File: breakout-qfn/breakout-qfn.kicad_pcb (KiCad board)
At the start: 2 copper layers, 50 x 52 mm, 153 parts, among them J1 Conn_01x04, J10 U.FL, J11 U.FL, J12 U.FL, J13 U.FL, J2 U.FL, J3 U.FL, J4 U.FL, J5 U.FL, J6 U.FL, J7 U.FL, J8 U.FL, J9 U.FL, U1 Openframe_QFN_TT06_REV2, U2 24LC02

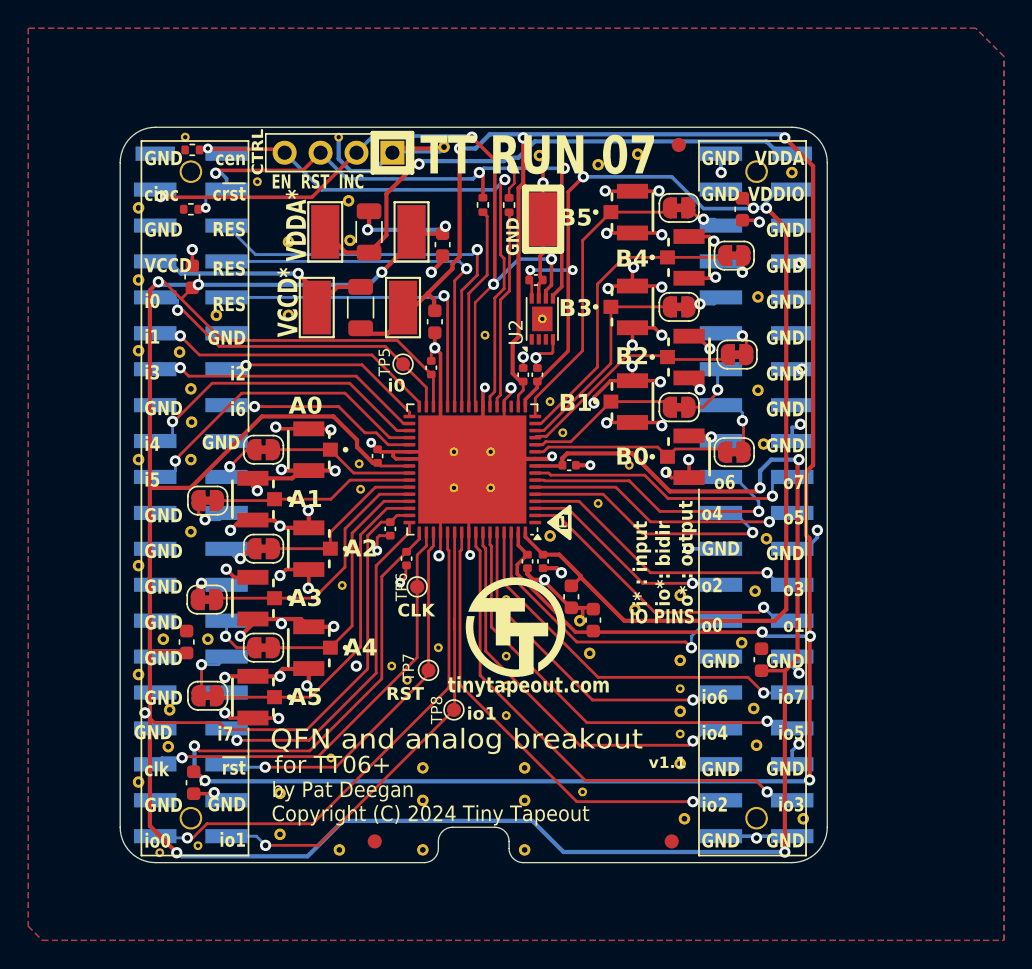
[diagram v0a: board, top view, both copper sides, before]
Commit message: TT08 breakout and documentation refactor
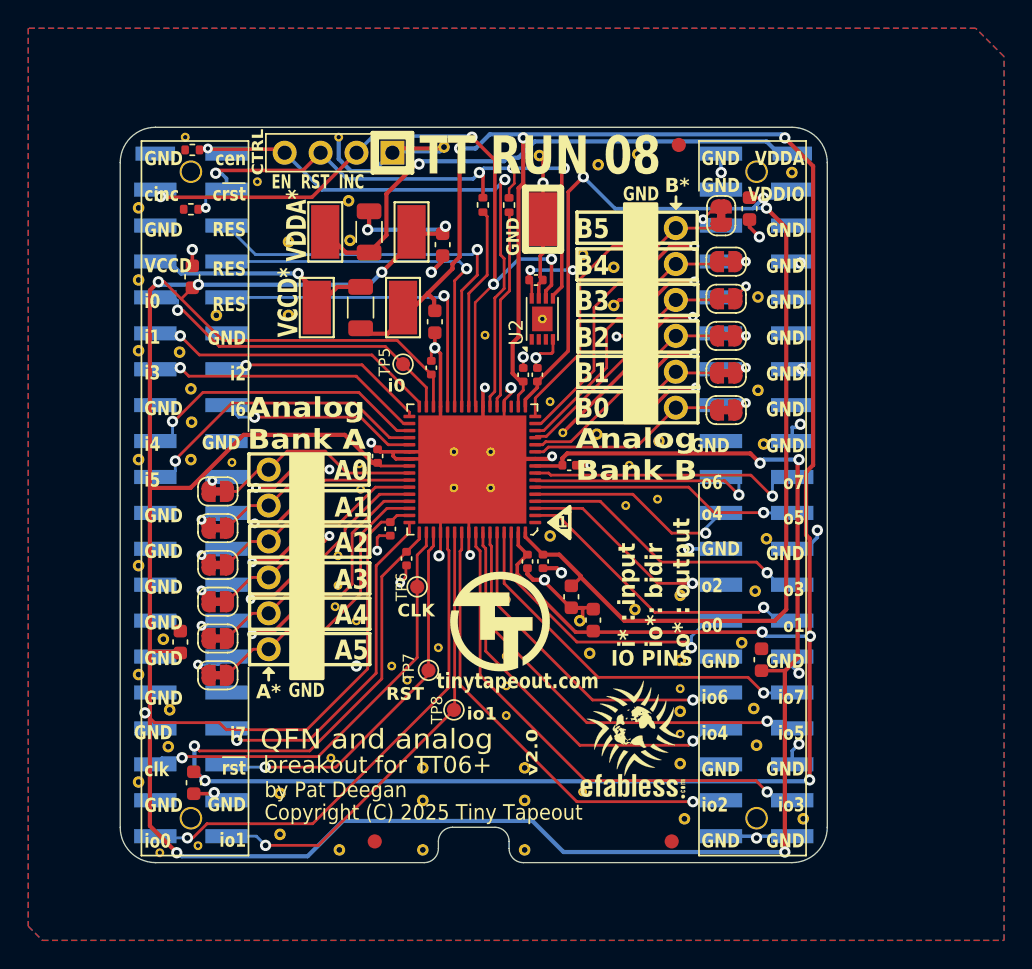
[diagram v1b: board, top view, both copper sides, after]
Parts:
- removed J10, J11, J12, J13, J4, J5, J6, J7, J8, J9: U.FL, psysnapeda:SAMTEC_RSP-122811-01
- removed the STITCHB1 at (50.5, 46.6)
- removed the STITCHB1 at (51.7, 54.2)
- added EFABLOG: Logo, TinyTapeout:ef_logo_graphical, F.Cu at (81.8, 60.5)
- added EFABLOG: Logo, TinyTapeout:ef_logo_graphical, B.Cu at (71.7, 64.1)
- added EFABTXT: Logo, TinyTapeout:ef_logo, F.Cu at (81.7, 64.6)
- added EFABTXT: Logo, TinyTapeout:ef_logo, B.Cu at (71.7, 60.0)
- added STITCHB1: StitchingVia-0.4mmDrill, flyingcarsfootprints:StitchingVia-0.4mmDrill, F.Cu at (83.6, 40.2)
- added STITCHB1: StitchingVia-0.4mmDrill, flyingcarsfootprints:StitchingVia-0.4mmDrill, F.Cu at (79.2, 39.7)
- added STITCHB1: StitchingVia-0.4mmDrill, flyingcarsfootprints:StitchingVia-0.4mmDrill, F.Cu at (80.4, 30.6)
- added STITCHB1: StitchingVia-0.4mmDrill, flyingcarsfootprints:StitchingVia-0.4mmDrill, F.Cu at (78.2, 27.0)
- added STITCHB1: StitchingVia-0.4mmDrill, flyingcarsfootprints:StitchingVia-0.4mmDrill, F.Cu at (80.4, 27.9)
- added STITCHM1: StitchingVia-0.3mm, flyingcarsfootprints:StitchingVia-0.3mm, F.Cu at (83.5, 44.3)
- added STITCHM1: StitchingVia-0.3mm, flyingcarsfootprints:StitchingVia-0.3mm, F.Cu at (60.9, 48.3)
- added STITCHM1: StitchingVia-0.3mm, flyingcarsfootprints:StitchingVia-0.3mm, F.Cu at (62.2, 52.9)
- added STITCHM1: StitchingVia-0.3mm, flyingcarsfootprints:StitchingVia-0.3mm, F.Cu at (53.4, 41.7)
- added STITCHM1: StitchingVia-0.3mm, flyingcarsfootprints:StitchingVia-0.3mm, F.Cu at (60.7, 51.9)
- J2, J3: value U.FL -> Conn_02x06_Odd_Even; footprint psysnapeda:SAMTEC_RSP-122811-01 -> Connector_PinHeader_2.54mm:PinHeader_2x06_P2.54mm_Vertical
- JP1, JP10, JP11, JP12, JP2, JP3, JP4, JP5, JP6, JP7, JP8, JP9: footprint Jumper:SolderJumper-2_P1.3mm_Bridged_RoundedPad1.0x1.5mm -> TinyTapeout:SolderJumper-2_P1.3mm_Bridged_RoundedPad1.0x1.5mmEasyCut
- moved J3 33.4 mm to (82.2, 25.1), turned to 0 degrees
- moved J2 14.1 mm to (58.5, 54.9), turned to 180 degrees
- moved JP1 4.38 mm to (52.4, 43.8)
- moved JP8 4.12 mm to (88.3, 35.4)
- moved JP3 3.44 mm to (52.4, 49.0)
- moved JP10 3.37 mm to (88.3, 30.1)
- moved JP5 3.30 mm to (52.4, 54.1)
- moved JP7 3.03 mm to (88.3, 38.0)
- moved JP12 3.03 mm to (88.0, 24.2), turned to 90 degrees
- moved Z2ALOGO01 2.81 mm to (61.4, 62.2)
- moved TTLOGO01 2.11 mm to (80.9, 62.6)
- moved JP2 2.08 mm to (52.4, 46.4)
- moved STITCHM1 1.96 mm to (81.2, 44.8)
- moved JP6 1.62 mm to (52.4, 56.8)
- moved JP9 1.54 mm to (88.3, 32.8)
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- renumbered REF** to TTLOGO01, REF** to Z2ALOGO01
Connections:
- J2 pad 1: /chip_an0 -> GND
- J3 pad 1: /chip_an1 -> GND
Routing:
- net GND: track 206.7 -> 180.3 mm, vias 69 -> 42
- net /uout4: track 19.5 -> 15.1 mm
- net /chip_an0: track 10.3 -> 14.7 mm
- net vdda_all: track 250.1 -> 245.9 mm
- net /chip_an7: track 11.0 -> 15.0 mm
- net /uout6: track 20.8 -> 17.2 mm
- net /chip_an5: track 23.8 -> 20.2 mm
- net /chip_an2: track 12.1 -> 15.2 mm
- net /chip_an9: track 15.5 -> 18.3 mm
- net /chip_an3: track 18.3 -> 16.3 mm
- net /chip_an11: track 21.0 -> 22.6 mm
- net /chip_an10: track 21.8 -> 20.2 mm
- net /chip_an4: track 17.8 -> 19.0 mm
- net /hd_an7: track 4.25 -> 3.05 mm
- net /hd_an0: track 3.06 -> 1.98 mm
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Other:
- board text added: "A*"
- board text added: "Analog Bank A"
- board text added: "Analog Bank B"
- board text added: "B*"
- board text added: "Copyright (C) 2025 Tiny Tapeout"
- board text added: "MUX CTRL"
- board text added: "QFN and analog"
- board text added: "TT RUN 08"
- board text added: "TT06+ QFN breakout v2"
- board text added: "TinyTapeout designs are packaged together along with a MUX that allows for directing I/O to any"
- board text added: "breakout for TT06+"
- board text added: "selected project, controlled through the cinc, cen and c~{rst} pins. This PCB provides a way to deliver these chips that will sit atop the demo board, but also allows you to easily integrate the ICs into your own projects. For details, see"
- board text added: "v2.0"
- board text removed: "Copyright (C) 2024 Tiny Tapeout"
- board text removed: "QFN and analog breakout"
- board text removed: "TT RUN 07"
- board text removed: "TT06+ QFN breakout v1"
- board text removed: "TinyTapeout designs are packaged together along with a MUX that allows for directing I/O to any selected project, controlled through the cinc, cen and c~{rst} pins. This PCB provides a way to deliver these chips that will sit atop the demo board, but also allows you to easily integrate the ICs into your own projects. For details, see"
- board text removed: "for TT06+"
- board text removed: "v1.1"

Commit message: minor routing tweaks and stitch
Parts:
- added STITCHB1: StitchingVia-0.4mmDrill, flyingcarsfootprints:StitchingVia-0.4mmDrill, F.Cu at (70.3, 60.8)
- added STITCHB1: StitchingVia-0.4mmDrill, flyingcarsfootprints:StitchingVia-0.4mmDrill, F.Cu at (58.2, 59.6)
- added STITCHB1: StitchingVia-0.4mmDrill, flyingcarsfootprints:StitchingVia-0.4mmDrill, F.Cu at (50.3, 44.4)
- added STITCHM1: StitchingVia-0.3mm, flyingcarsfootprints:StitchingVia-0.3mm, F.Cu at (77.8, 45.7)
- added STITCHM1: StitchingVia-0.3mm, flyingcarsfootprints:StitchingVia-0.3mm, F.Cu at (79.3, 45.2)
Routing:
- net GND: track 180.3 -> 194.5 mm
- net vdda_in: track 39.0 -> 40.1 mm
- net vccd_in: track 17.1 -> 18.0 mm
- net /uio1: track 33.8 -> 33.0 mm
- net vdda_all: track 245.9 -> 245.2 mm, vias 10 -> 9

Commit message: routing tweaks
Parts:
- moved STITCHB1 1.45 mm to (88.0, 54.5)
- moved STITCHB1 0.65 mm to (90.5, 47.1)
- moved STITCHB1 0.47 mm to (90.5, 40.2)
- moved STITCHB1 0.38 mm to (93.5, 66.8)
- moved STITCHM1 0.38 mm to (83.2, 44.1)
- moved STITCHB1 0.35 mm to (48.6, 59.2)
- moved STITCHB1 0.25 mm to (48.6, 61.8)
- moved STITCHM1 0.20 mm to (81.0, 44.8)
- moved STITCHM1 0.20 mm to (60.7, 50.4)
- moved STITCHB1 0.16 mm to (46.8, 23.6)
- moved STITCHB1 0.11 mm to (85.5, 66.8)
- moved STITCHM1 0.10 mm to (55.2, 21.9)
- moved STITCHB1 0.10 mm to (48.5, 54.2)
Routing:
- net GND: track 194.5 -> 280.0 mm

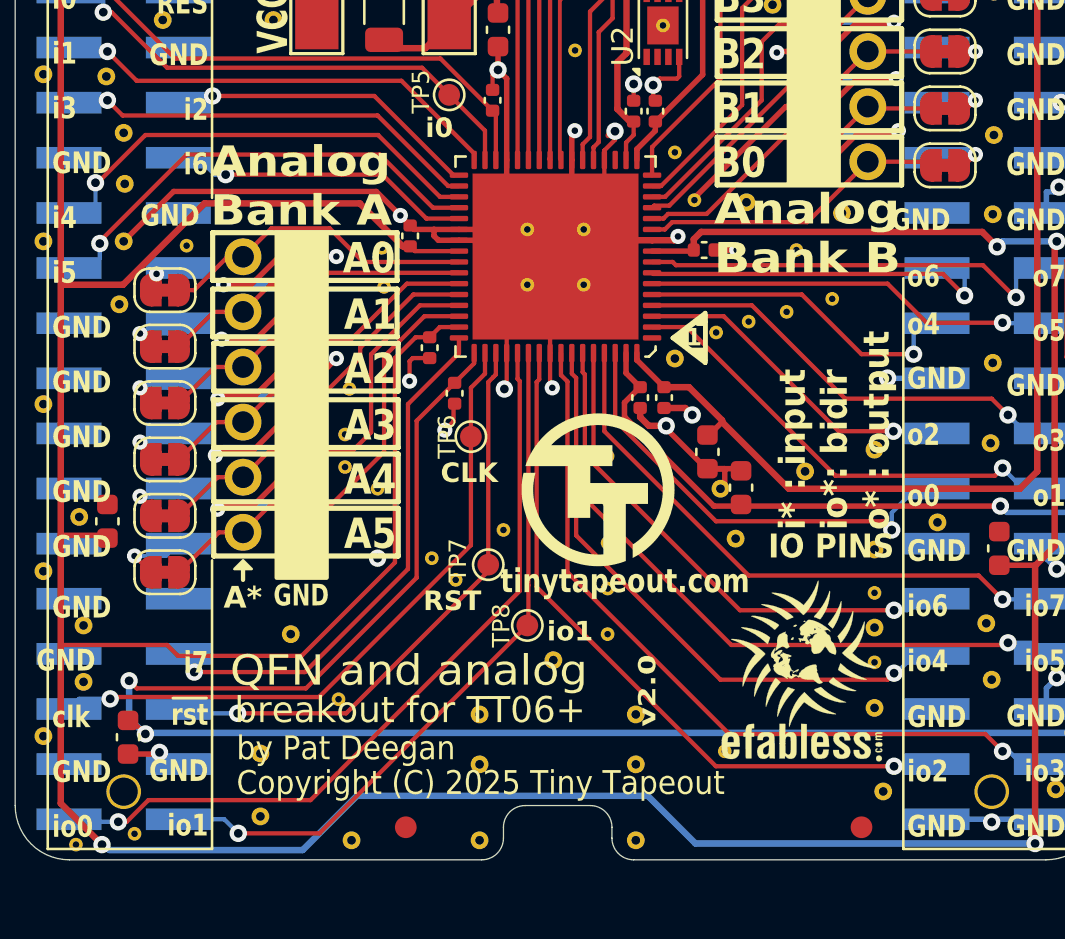
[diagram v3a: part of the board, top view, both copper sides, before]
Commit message: Fab layer cleanup and BOM MPNs
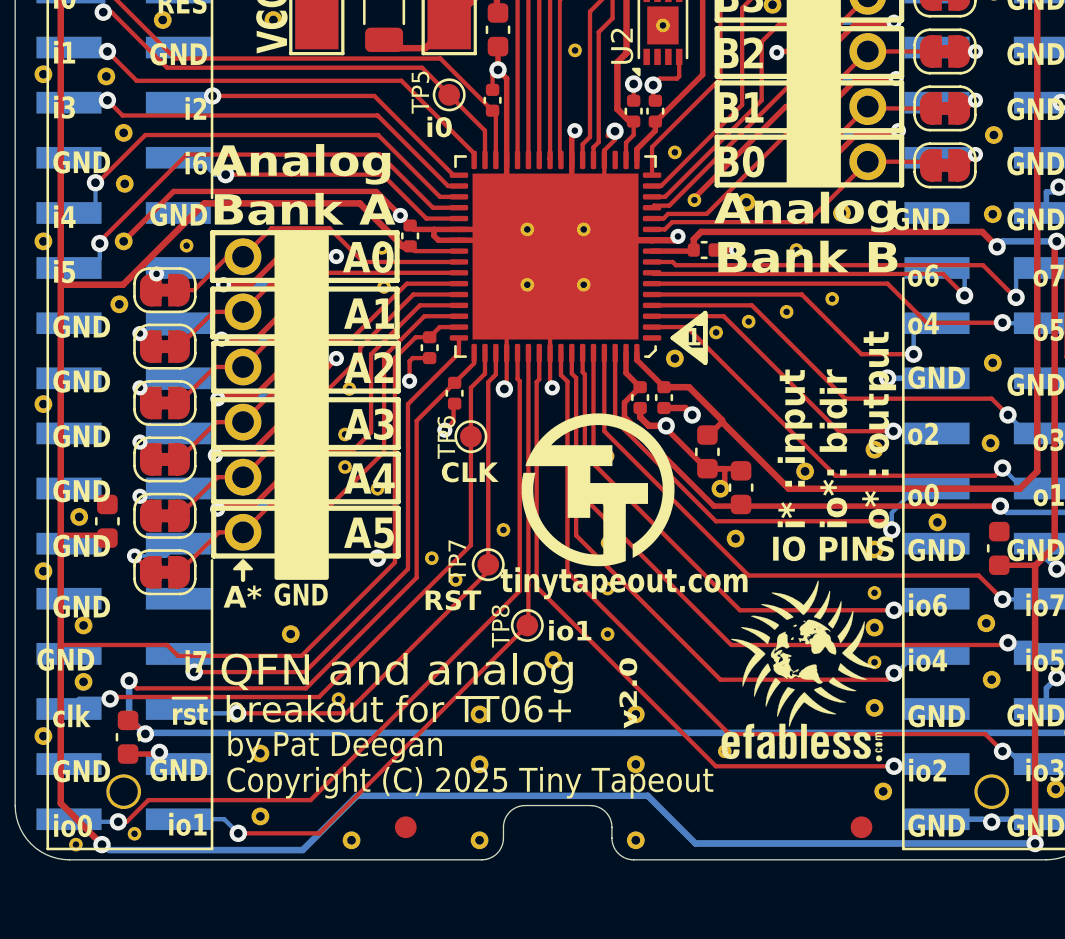
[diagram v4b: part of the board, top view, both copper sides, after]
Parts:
- CON1, CON2: value ~ -> NPTC202KFMS-RC
- renumbered EFABLOG to EFABLOG1, EFABLOG to EFABLOG2, EFABTXT to EFABTXT1, EFABTXT to EFABTXT2, G*** to PSYLOGO1, TTLOGO to TTLOGO1
